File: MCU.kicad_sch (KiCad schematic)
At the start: 28 parts, among them J4 Conn_01x12_MountingPin, Q5 MMBT3904, Q6 MMBT3904, SW1 SW_DPDT_x2, SW2 PTS647SN50SMTR2_LFS, SW3 PTS647SN50SMTR2_LFS, U4 CP2102N-Axx-xQFN28, U5 ESP32-C3-WROOM-02, U6 LIS3DH

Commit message: setup layout rules
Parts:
- removed J4: Conn_01x12_MountingPin, Connector_PinHeader_2.54mm:PinHeader_1x12_P2.54mm_Vertical, symbol Connector_Generic_MountingPin:Conn_01x12_MountingPin
- added J5: Conn_01x12, Connector_PinHeader_2.54mm:PinHeader_1x12_P2.54mm_Vertical, symbol Connector_Generic:Conn_01x12
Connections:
- net GD_INT: now also J5.10 (Pin_10)
- net GND: now also J5.12 (Pin_12)
- net I2C1_SCL: now also J5.2 (Pin_2)
- net I2C1_SDA: now also J5.1 (Pin_1)
- net RXD: now also J5.8 (Pin_8)
- net SPI2_MISO: now also J5.3 (Pin_3)
- net SPI2_MOSI: now also J5.5 (Pin_5)
- net SPI2_SCLK: now also J5.4 (Pin_4)
- net THIEF_INT: now also J5.9 (Pin_9)
- net TXD: now also J5.7 (Pin_7)
- net ~{GD_SAFE}: now also J5.11 (Pin_11)
- net ~{SPI2_CS}: now also J5.6 (Pin_6)

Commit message: first pass layout
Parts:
- added C22: 4.7uF, Capacitor_SMD:C_0603_1608Metric, symbol Device:C
- added C23: 0.1uF, Capacitor_SMD:C_0603_1608Metric, symbol Device:C
- U5: footprint RF_Module:ESP32-C3-WROOM-02 -> custom_footprints:ESP32-C3-WROOM
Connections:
- net +3V3: now also C22.1, C23.1
- net GND: now also C22.2, C23.2

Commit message: Did some more routing
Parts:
- R35: value 5.1k -> 3.7k
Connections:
- net DTR: now also Q6.2 (E)
- net RTS: now also Q5.2 (E)
- net at Q5.1 (B), R30.1: no longer Q6.2 (E)
- net at Q6.1 (B), R31.1: no longer Q5.2 (E)
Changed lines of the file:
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@@
 	)
 	(junction
-		(at 161.29 181.61)
+		(at 97.79 60.96)
 		(diameter 0)
 		(color 0 0 0 0)
 	)
 	(junction
-		(at 97.79 60.96)
+		(at 35.56 175.26)
 		(diameter 0)
 		(color 0 0 0 0)
 	)
 	(junction
-		(at 162.56 198.12)
+		(at 85.09 60.96)
 		(diameter 0)
 		(color 0 0 0 0)
 	)
 	(junction
-		(at 35.56 175.26)
+		(at 146.05 181.61)
 		(diameter 0)
 		(color 0 0 0 0)
 	)
 	(junction
-		(at 85.09 60.96)
+		(at 147.32 198.12)
 		(diameter 0)
 		(color 0 0 0 0)
@@
 	(wire
 		(pts
-			(xy 85.09 83.82) (xy 85.09 90.17)
+			(xy 146.05 191.77) (xy 146.05 181.61)
 		)
 		(stroke
@@
 	(wire
 		(pts
-			(xy 116.84 83.82) (xy 143.51 83.82)
+			(xy 146.05 181.61) (xy 152.4 181.61)
+		)
+		(stroke
+			(width 0)
+			(type default)
+		)
+	)
+	(wire
+		(pts
+			(xy 85.09 83.82) (xy 85.09 90.17)
 		)
 		(stroke
@@
 	(wire
 		(pts
-			(xy 162.56 187.96) (xy 170.18 187.96)
+			(xy 116.84 83.82) (xy 143.51 83.82)
 		)
 		(stroke
@@
 	(wire
 		(pts
+			(xy 146.05 191.77) (xy 170.18 191.77)
+		)
+		(stroke
+			(width 0)
+			(type default)
+		)
+	)
+	(wire
+		(pts
 			(xy 35.56 195.58) (xy 35.56 203.2)
 		)
@@
 	(wire
 		(pts
+			(xy 147.32 187.96) (xy 147.32 198.12)
+		)
+		(stroke
+			(width 0)
+			(type default)
+		)
+	)
+	(wire
+		(pts
 			(xy 190.5 228.6) (xy 193.04 228.6)
 		)
@@
 	(wire
 		(pts
-			(xy 135.89 198.12) (xy 152.4 198.12)
+			(xy 135.89 198.12) (xy 147.32 198.12)
 		)
 		(stroke
@@
 	(wire
 		(pts
+			(xy 147.32 198.12) (xy 152.4 198.12)
+		)
+		(stroke
+			(width 0)
+			(type default)
+		)
+	)
+	(wire
+		(pts
 			(xy 22.86 165.1) (xy 22.86 175.26)
 		)
@@
 	(wire
 		(pts
-			(xy 135.89 181.61) (xy 152.4 181.61)
+			(xy 135.89 181.61) (xy 146.05 181.61)
 		)
 		(stroke
@@
 	(wire
 		(pts
-			(xy 295.91 129.54) (xy 295.91 142.24)
+			(xy 147.32 187.96) (xy 170.18 187.96)
 		)
 		(stroke
@@
 	(wire
 		(pts
-			(xy 72.39 83.82) (xy 72.39 90.17)
+			(xy 295.91 129.54) (xy 295.91 142.24)
 		)
 		(stroke
@@
 	(wire
 		(pts
-			(xy 193.04 213.36) (xy 193.04 207.01)
+			(xy 72.39 83.82) (xy 72.39 90.17)
 		)
 		(stroke
@@
 	(wire
 		(pts
-			(xy 295.91 149.86) (xy 295.91 172.72)
+			(xy 193.04 213.36) (xy 193.04 207.01)
 		)
 		(stroke
@@
 	(wire
 		(pts
-			(xy 60.96 86.36) (xy 60.96 99.06)
+			(xy 295.91 149.86) (xy 295.91 172.72)
 		)
 		(stroke
@@
 	(wire
 		(pts
-			(xy 129.54 101.6) (xy 143.51 101.6)
+			(xy 60.96 86.36) (xy 60.96 99.06)
 		)
 		(stroke
@@
 	(wire
 		(pts
-			(xy 161.29 181.61) (xy 160.02 181.61)
+			(xy 129.54 101.6) (xy 143.51 101.6)
 		)
 		(stroke
@@
 	(wire
 		(pts
-			(xy 161.29 191.77) (xy 170.18 191.77)
-		)
-		(stroke
-			(width 0)
-			(type default)
-		)
-	)
-	(wire
-		(pts
 			(xy 62.23 147.32) (xy 80.01 147.32)
 		)
@@
 	(wire
 		(pts
-			(xy 161.29 191.77) (xy 161.29 181.61)
-		)
-		(stroke
-			(width 0)
-			(type default)
-		)
-	)
-	(wire
-		(pts
 			(xy 80.01 125.73) (xy 97.79 125.73)
 		)
@@
 	(wire
 		(pts
-			(xy 162.56 187.96) (xy 162.56 198.12)
-		)
-		(stroke
-			(width 0)
-			(type default)
-		)
-	)
-	(wire
-		(pts
 			(xy 193.04 180.34) (xy 195.58 180.34)
 		)
@@
 	(wire
 		(pts
-			(xy 161.29 181.61) (xy 162.56 181.61)
+			(xy 160.02 181.61) (xy 162.56 181.61)
 		)
 		(stroke
@@
 			)
 		)
-		(property "Value" "5.1k"
+		(property "Value" "3.7k"
 			(at 227.584 227.33 90)
 			(effects

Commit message: route dc-dc
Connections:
- net GD_SAFE is gone; now on net ~{GD_SAFE}: Q6.3 (C), SW3.1 (NO_1), SW3.2 (NO_2)
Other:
- moved on the sheet: R34, R35
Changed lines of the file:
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@@
 	)
 	(junction
-		(at 233.68 220.98)
+		(at 35.56 45.72)
 		(diameter 0)
 		(color 0 0 0 0)
@@
 	(wire
 		(pts
-			(xy 233.68 237.49) (xy 233.68 231.14)
+			(xy 35.56 62.23) (xy 35.56 55.88)
 		)
 		(stroke
@@
 	(wire
 		(pts
-			(xy 233.68 217.17) (xy 233.68 220.98)
+			(xy 35.56 41.91) (xy 35.56 45.72)
 		)
 		(stroke
@@
 	(wire
 		(pts
-			(xy 233.68 220.98) (xy 233.68 223.52)
+			(xy 35.56 45.72) (xy 35.56 48.26)
 		)
 		(stroke
@@
 	(wire
 		(pts
-			(xy 233.68 201.93) (xy 233.68 209.55)
+			(xy 35.56 26.67) (xy 35.56 34.29)
 		)
 		(stroke
@@
 	(wire
 		(pts
-			(xy 246.38 220.98) (xy 233.68 220.98)
+			(xy 48.26 45.72) (xy 35.56 45.72)
 		)
 		(stroke
@@
 			"ZABPAHkALwB0AHMASQBzAFMAVQBoACsAdwA1ACsAMwBIAEoAWAB4AEkAUAA3AGgANgBDAHgAKwAw"
 			"AC8AQwBaAHQAeQAvAFMAagBNAHUAaAA3AEwAUgByAGQAZAB0AG0ARABWAHQASAB6AG4AMgB3AHgA"
-			"Wg=="
+			"WgAzAHUAdQAzAGUAQQBrADQAaABNAEQAaQBHAG0AMQA5AEwAYwBaAEIAcgBXAFAAVABwAC8ANgAw"
+			"AEIAVwBIAGIAZQBaAHMAcgBTAHgASQBmAGgAeABWAC8AYgBFAEUAUgBXAGIANQArADgAYQBvAEQA"
+			"UABFAFkATQA4AEIAcgByAEcAbABCACsATQAzAGcAcABsAGwARQBXAHMAeQBUAEUAcQA2AEoAWQAz"
+			"ADkAbABvAFIAcABpAFQATQBmAHAAMwA1AHUAMABHAGsAZwBGAFkALwBWAHoAYwA5AFUAaABTAHAA"
+			"OABtAHYAUgBHADkATgBTAFUATgBGAFoASABGAGwAUgB4AGIAQgA5AGMANQBVAHcAYQAwADIAcwBQ"
+			"AEkAMgByAG8ANgAxAEYAQgBhADkAUABGAHYASQB2ADMAeQBzAFoAQQBLAGQAYwArAE4AYQA2ADEA"
+			"RgA3AEkAMABzAHEAMABYAHIAMwBGAFIARgBCAGkAVgBhAFQAZQBiAGgAUQBkAHcAVwBCADYASgA4"
+			"AEQAMAB1AFgAKwBiACsASABjAGkAZQBjAHYAUgBlAHcAbwBWAC8AVABxADIAdABFACsAdQBYAEQA"
+			"ZwBhAFcAcQBFAHoAZAB2AHQASgBjAFIAcwBTAGoAcABQAGkAdQAzAHoAZABZAHMAagBqAHAAMQBL"
+			"AGIAWgB4AHoAMgBuAEkAdgBuAEEANgBvAE0ASABBAFkAOABzAEsAWgB4AEcASABNADgAWQAwAFgA"
+			"NwBKAGoAdgBpADQAdgA4AHUATABwADIARwArADEAVwB4AFEAQQBBAEkAQgAyAGcAYgA0AGYALwA5"
+			"AE0AbwB3AGQATQA5AFAANgB3AEoATABVAFMAdAA4AGcAeQBxADUATQBYAFIAMQBlAHUARwAyAFoA"
+			"NgBkAG8AUABCAFYAVQBsAFIAWgBDAC8AZQBmAHoANwB0AHYAMgB2ADgAcQA2AE4AbwBWADcANgB2"
+			"AFgALwBQADAATwByADcAMQB4ADUAQgBmAGoAWQBUADkAcwAyAHIAVgBwAFcAbgAvAGwAbAB1AHYA"
+			"RQBaAEsAMABuAGYARwBlAG4AMABYAFMAcgBSAHcAbgBxAHEAOABzAEwATQBsADcASAB4AHoANgAv"
+			"AHMAdABDADEATgBPAFAAWQAyAGYAVQB1ADYAcAA5AGUASQBpAGMASgBnAHEAUwBhADEAdwBuAEQA"
+			"YwBCAHEAdAArAFcATABiAEcAMABOAHAAUgBHAGcAaQBYADMAUAB1AGgATQBHAGkAYgBnADAAUgBR"
+			"AGkAeQBiAFUAUwBOAFUARABuAG8ALwBqAGkAdwBpAEwAWgB2ADYAawBuAEEAVQBsAFQANAAzAHAA"
+			"ag=="
 		)
 	)
@@
 			"cUpacDduUDV3ZjNraVNxQ3JRdlA4V3U4OUptWERuOWNGZTFXZFg5U0R6eHZ3K3N5Sm4zWWplN3Q1"
 			"NGZsT1pYcjkzWHhZeE55OXE5L2ZVUWhja2YzejNQaklwVDBpb08vWHNhcVZVVitHVmsvdmY0dTZM"
-			"UA=="
+			"UHJ0ZnNscnI0K1B0elI0RHVqRHA4bXFhS2t3Wk5VUDcyVHNEYzRRMFNGUCs0My9uampSVlowZ3Jx"
+			"cXNyeTBnckdBNTIzK1NmWENQaFJJQ1ZFYlJyNW5CakpZYXNzcnFhckpSY045dkpXNisvcXhXYUN5"
+			"czc3Ti9aanFacTBnd2xkUTBsR1NubGJnT25iYno1cnZwN2ROOFhZUjNIYlh0YUJVcGZIM2I1SXEz"
+			"RG1EVytCVi9tenR5cU56NXJKMWpwSzhncGZsR2ppdW5RMlVmQ0NualZ5RW83TTN2MG1IWCtud1ZW"
+			"QkMrOHU4SnA5S3lMS1FKcldYRm5yYU9EdzlqTmp4bzUzTVFEN2w5S2Q1ejZ6d3NoRXJGakQ3dVBI"
+			"ajMzV3ByUUFFVUMrM0IycnFPVHg5R2tieFlsamdoOFlDbm5QY2VNV1JGUUtLZ2d2TVRmZTlRNHp6"
+			"TjhQN1N2OFBZUnE0UFVQdGc0YXR3Y240L2NobmUzTjduYjZjdEpNZFUwVlpreVN0M3RQSGJkRlRZ"
+			"dVNHby9naUc0UmVISEY0eXgxSlJoS0tocnFpbklLbmJ0NTdyKy9PdHl3ZDRXVmhSemNxbXpsYTRj"
+			"WFU1VlE1WEprTlBzUFhiZWdmQmNGbDlLY1lYQ0srK3RkaHJwNERCdVJ4akc1YnpaTzlHQmp6RXJy"
+			"K1cyeWIweEozRFg3S0hHeWxKeXlocXFDZ3g1WFJ2M05WZFRxb215d0RWT28yYWNULzZxQlFKTFBl"
+			"UGw2THppVnJFZ3RYQkxiNjkwR3JYZzlIdmVPbytmZCtsdHF0OWFsNzdkTkZXMHUzdmN6UC9TM0ho"
+			"NS9BVnZWeXM5UlJrbGRTME5GU1pUcFlmRHJQMlIrUzEySjlyNGF4OXNIT1UwOWJzWnQ4QXBlWEZ5"
+			"eFhnclBSbUdyS3FHR3BNaHJXazFhdjdSeC9sOEN1MllrVUFnRUVobkFvT3YvbmdJTnBjREFBQmtw"
+			"cUk4aWVkeFk4cVpXVTRyL1BPYlcrWXdCRlpYbFBUSUp5bkU5OHJjMHdHSC9qSnNMMUtyK3NWZVo3"
+			"Zk5VWjg1MzdJZ1dFWHZIaDlkRnY3QTEwcmNBNWs1K1FtaG9lbTFsUGlOWVdXR1RoT1hlK2hJVmFa"
+			"SFA3amp2OFgxUmNycE8yNVAvcHA4dmJqYmNEZHZUMk5tYzJGcWRQRGRvd3VIeENUNVBUZzVWdTJi"
+			"ODB0d015N09ITEh3Umo1TjEzN0NvbG05OU9YWjVaa0pvYmN2cmgzMTdMVlBzTzgwdlcrQ3N3cGVo"
+			"b1ZtRnBVR3ZrMnVWVGZxMFVXVHBLbXRKbFJ6M0t6THN4d1grellOM3g3MGw2MHNBQURneFFGTEIw"
+			"MA=="
 		)
 	)
@@
 	)
 	(label "48V_ADC"
-		(at 246.38 220.98 180)
+		(at 48.26 45.72 180)
 		(effects
 			(font
@@
 		)
 	)
-	(label "GD_SAFE"
+	(label "~{GD_SAFE}"
 		(at 191.77 207.01 180)
 		(effects
@@
 	(symbol
 		(lib_id "power:GND")
-		(at 233.68 237.49 0)
+		(at 35.56 62.23 0)
 		(unit 1)
 		(exclude_from_sim no)
@@
 		(dnp no)
 		(property "Reference" "#PWR0151"
-			(at 233.68 243.84 0)
+			(at 35.56 68.58 0)
 			(effects
 				(font
@@
 		)
 		(property "Value" "GND"
-			(at 233.68 242.57 0)
+			(at 35.56 67.31 0)
 			(effects
 				(font
@@
 		)
 		(property "Footprint" ""
-			(at 233.68 237.49 0)
+			(at 35.56 62.23 0)
 			(effects
 				(font
@@
 		)
 		(property "Datasheet" ""
-			(at 233.68 237.49 0)
+			(at 35.56 62.23 0)
 			(effects
 				(font
@@
 		)
 		(property "Description" "Power symbol creates a global label with name \"GND\" , ground"
-			(at 233.68 237.49 0)
+			(at 35.56 62.23 0)
 			(effects
 				(font
@@
 	(symbol
 		(lib_id "Device:R")
-		(at 233.68 213.36 180)
+		(at 35.56 38.1 180)
 		(unit 1)
 		(exclude_from_sim no)
@@
 		(dnp no)
 		(property "Reference" "R34"
-			(at 230.124 213.36 90)
+			(at 32.004 38.1 90)
 			(effects
 				(font
@@
 		)
 		(property "Value" "75k"
-			(at 227.584 213.36 90)
+			(at 29.464 38.1 90)
 			(effects
 				(font
@@
 		)
 		(property "Footprint" "Resistor_SMD:R_0603_1608Metric"
-			(at 235.458 213.36 90)
+			(at 37.338 38.1 90)
 			(effects
 				(font
@@
 		)
 		(property "Datasheet" "~"
-			(at 233.68 213.36 0)
+			(at 35.56 38.1 0)
 			(effects
 				(font
@@
 		)
 		(property "Description" "Resistor"
-			(at 233.68 213.36 0)
+			(at 35.56 38.1 0)
 			(effects
 				(font
@@
 	(symbol
 		(lib_id "Device:R")
-		(at 233.68 227.33 180)
+		(at 35.56 52.07 180)
 		(unit 1)
 		(exclude_from_sim no)
@@
 		(dnp no)
 		(property "Reference" "R35"
-			(at 230.124 227.33 90)
+			(at 32.004 52.07 90)
 			(effects
 				(font
@@
 		)
 		(property "Value" "3.7k"
-			(at 227.584 227.33 90)
+			(at 29.464 52.07 90)
 			(effects
 				(font
@@
 		)
 		(property "Footprint" "Resistor_SMD:R_0603_1608Metric"
-			(at 235.458 227.33 90)
+			(at 37.338 52.07 90)
 			(effects
 				(font
@@
 		)
 		(property "Datasheet" "~"
-			(at 233.68 227.33 0)
+			(at 35.56 52.07 0)
 			(effects
 				(font
@@
 		)
 		(property "Description" "Resistor"
-			(at 233.68 227.33 0)
+			(at 35.56 52.07 0)
 			(effects
 				(font
@@
 	(symbol
 		(lib_id "power:+3V3")
-		(at 233.68 201.93 0)
+		(at 35.56 26.67 0)
 		(unit 1)
 		(exclude_from_sim no)
@@
 		(fields_autoplaced yes)
 		(property "Reference" "#PWR0149"
-			(at 233.68 205.74 0)
+			(at 35.56 30.48 0)
 			(effects
 				(font
@@
 		)
 		(property "Value" "BAT+"
-			(at 233.68 196.85 0)
+			(at 35.56 21.59 0)
 			(effects
 				(font
@@
 		)
 		(property "Footprint" ""
-			(at 233.68 201.93 0)
+			(at 35.56 26.67 0)
 			(effects
 				(font
@@
 		)
 		(property "Datasheet" ""
-			(at 233.68 201.93 0)
+			(at 35.56 26.67 0)
 			(effects
 				(font
@@
 		)
 		(property "Description" "Power symbol creates a global label with name \"+3V3\""
-			(at 233.68 201.93 0)
+			(at 35.56 26.67 0)
 			(effects
 				(font

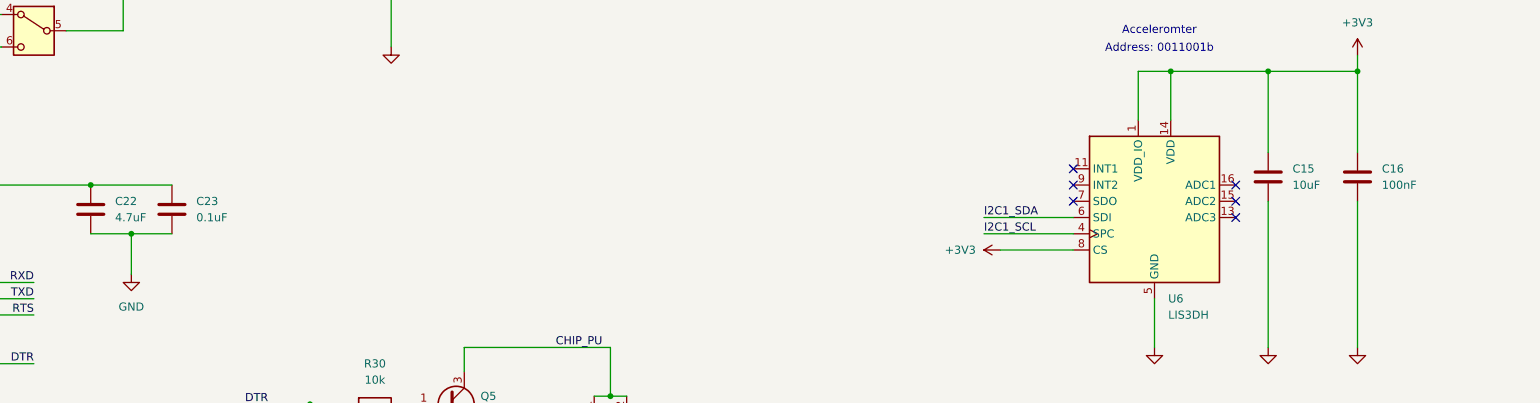
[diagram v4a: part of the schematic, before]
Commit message: More routing, changed the footprints of some caps.
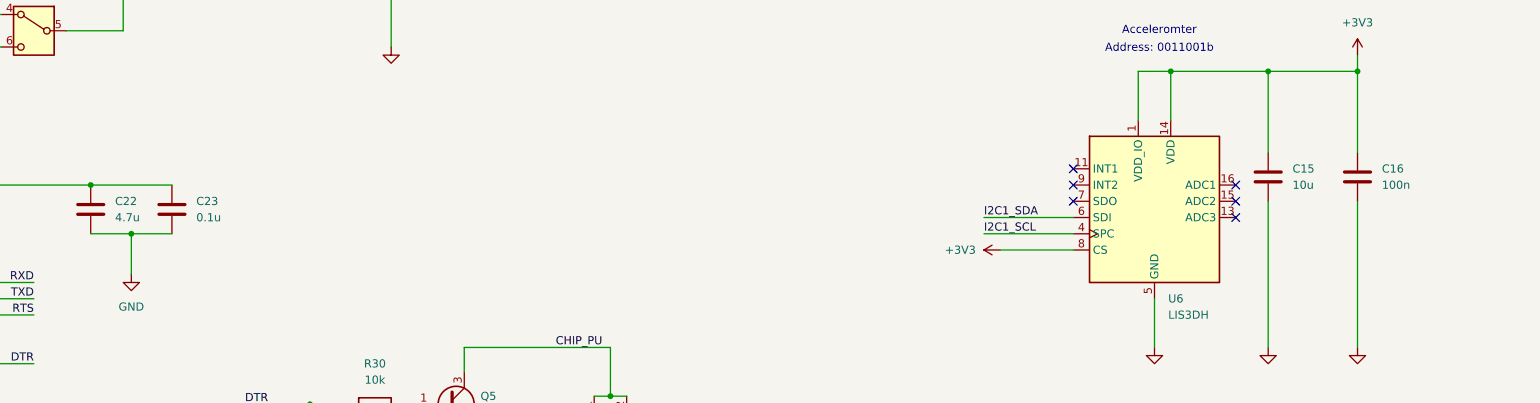
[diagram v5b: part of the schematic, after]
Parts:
- C15: value 10uF -> 10u
- C16: value 100nF -> 100n
- C22: value 4.7uF -> 4.7u
- C23: value 0.1uF -> 0.1u
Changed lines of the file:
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@@
 			)
 		)
-		(property "Value" "100nF"
+		(property "Value" "100n"
 			(at 313.69 147.3199 0)
 			(effects
@@
 			)
 		)
-		(property "Value" "4.7uF"
+		(property "Value" "4.7u"
 			(at 115.57 152.3999 0)
 			(effects
@@
 			)
 		)
-		(property "Value" "10uF"
+		(property "Value" "10u"
 			(at 299.72 147.3199 0)
 			(effects
@@
 			)
 		)
-		(property "Value" "0.1uF"
+		(property "Value" "0.1u"
 			(at 128.27 152.3999 0)
 			(effects
